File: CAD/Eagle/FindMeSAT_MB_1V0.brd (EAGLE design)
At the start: 99 x 49.2 mm, 128 parts, among them J291 MCX-J-P-X-RA-SM1, J685 SMA_CON, J701 MOLEX_105017-0001, J801 MICROSIM-8P_SDCARD-8P_MOLEX-1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, J901 JST_S3B-XH-A, Q101 ABS07-32.768KHZ, Q651 ABM3B-16MHZ-10-R50-1-U, U1001 CFPT-141-20MHZ, U101 ATXMEGA256A3BU-AU, U1011 OPA354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

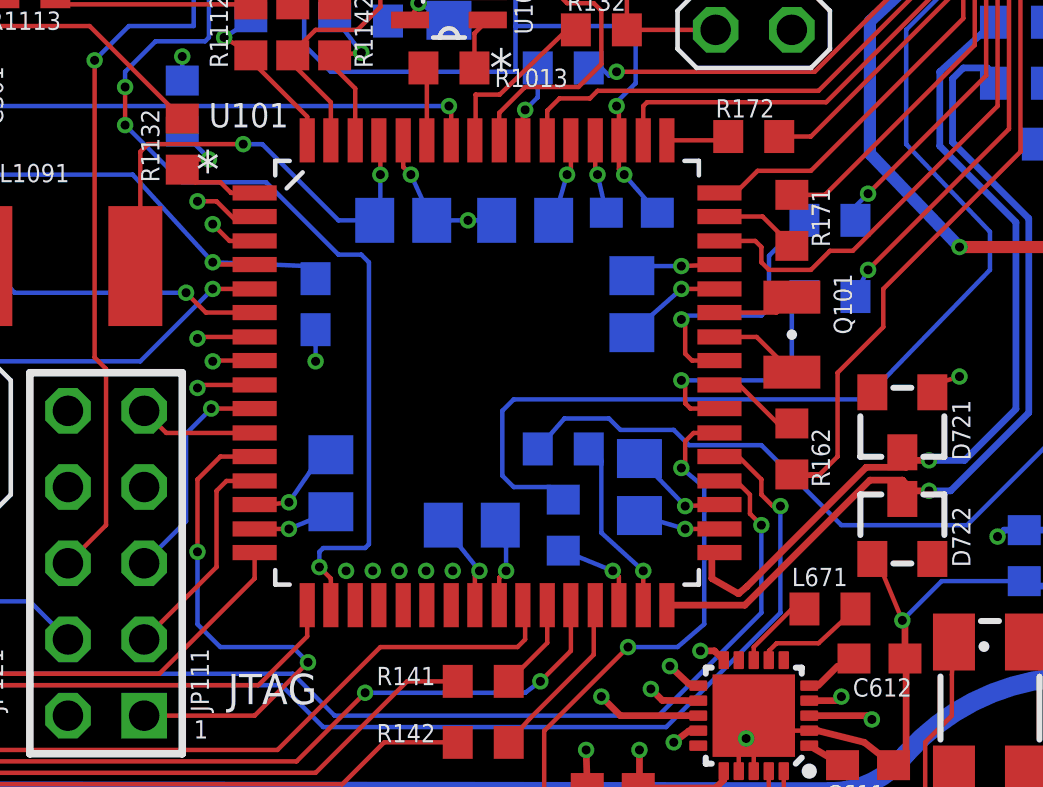
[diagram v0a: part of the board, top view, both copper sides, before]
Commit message: Eagle - I/O header needs OC1A for digital clock output, USB_ID gives way and goes to ADC1/ADC9/AC1 port
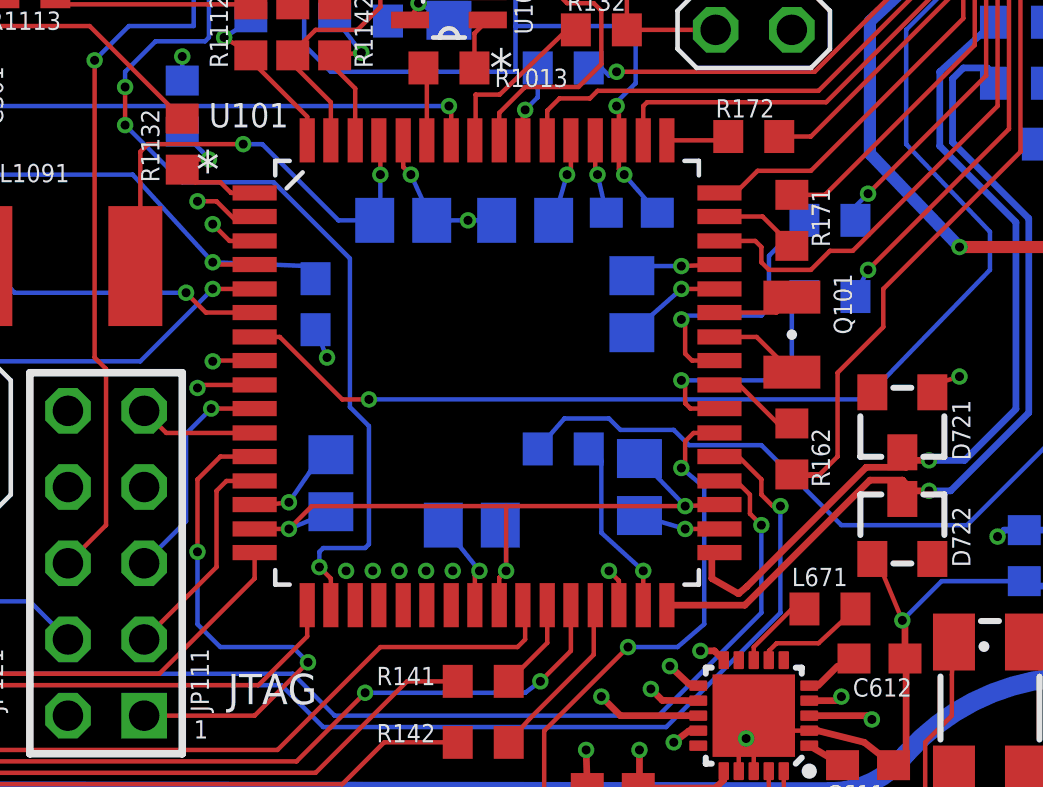
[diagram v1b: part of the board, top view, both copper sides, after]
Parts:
- removed R151: 27R, rcl:R0603
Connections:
- net IO_AD1 renamed IO_ADC4
- net IO_AD2 renamed IO_ADC5
- net IO_D2 renamed IO_DAC0
- net IO_D3 renamed IO_DAC1
- removed net IO_D1: JP181.2, U101.7
- removed net USB_ID_DRV: R151.1, U101.30
- new net IO_OC1A: JP181.2, U101.30
- net USB_ID: now also U101.7; no longer R151.2
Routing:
- net IO_OC1A: track 0.00 -> 29.0 mm, vias 0 -> 1
- net +3V3: track 69.9 -> 85.5 mm
- net IO_D1: track 12.8 -> 0.00 mm, vias 1 -> 0
- net USB_ID: track 38.0 -> 42.5 mm, vias 0 -> 1
- net USB_ID_DRV: track 3.01 -> 0.00 mm, vias 1 -> 0

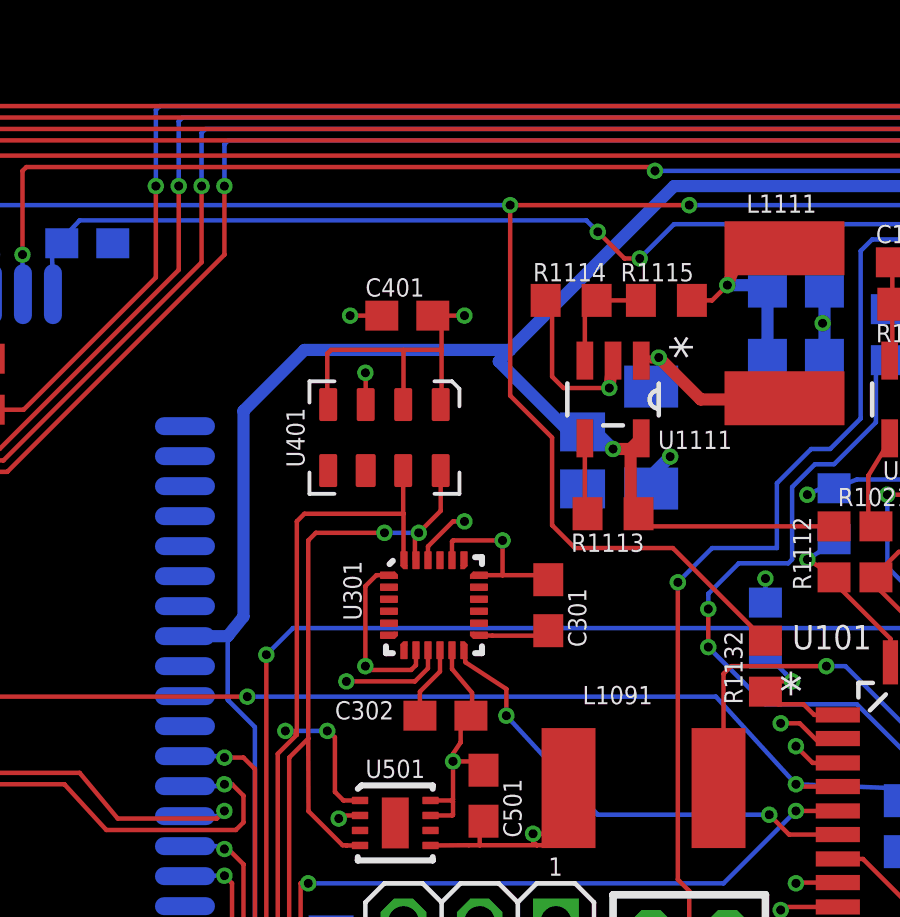
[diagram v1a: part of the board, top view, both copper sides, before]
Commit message: Eagle - I2C bus terminated
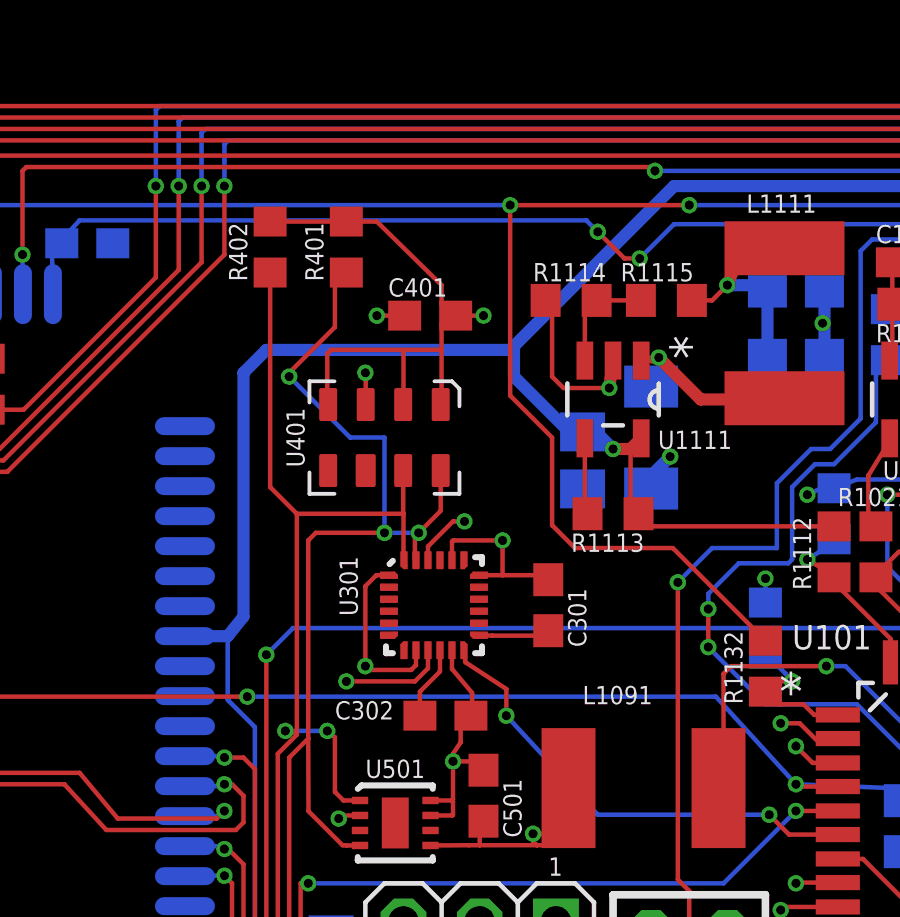
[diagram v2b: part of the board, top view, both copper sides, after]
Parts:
- added R401, R402: 10kR, rcl:R0603
- R211, R212: value 3.3kR -> 10kR
- moved C401 0.76 mm to (49.8, 34.5)
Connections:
- net +3V3: now also R401.2, R402.2
- net SCL1: now also R401.1
- net SDA1: now also R402.1
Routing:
- net SCL1: track 98.9 -> 110.3 mm, vias 7 -> 8
- net SDA1: track 96.1 -> 104.6 mm
- net +3V3: track 85.5 -> 93.5 mm
- net +5V: track 129.1 -> 129.6 mm

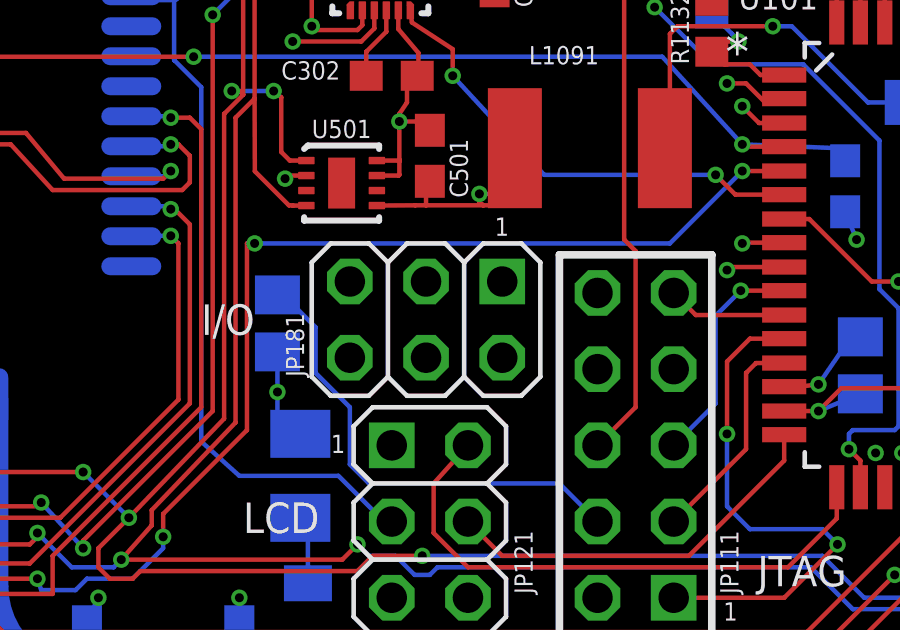
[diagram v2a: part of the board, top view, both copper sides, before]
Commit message: Eagle - dis-parted +3V3 layer by signal lines bridged, Beta-LAYOUT previews updated
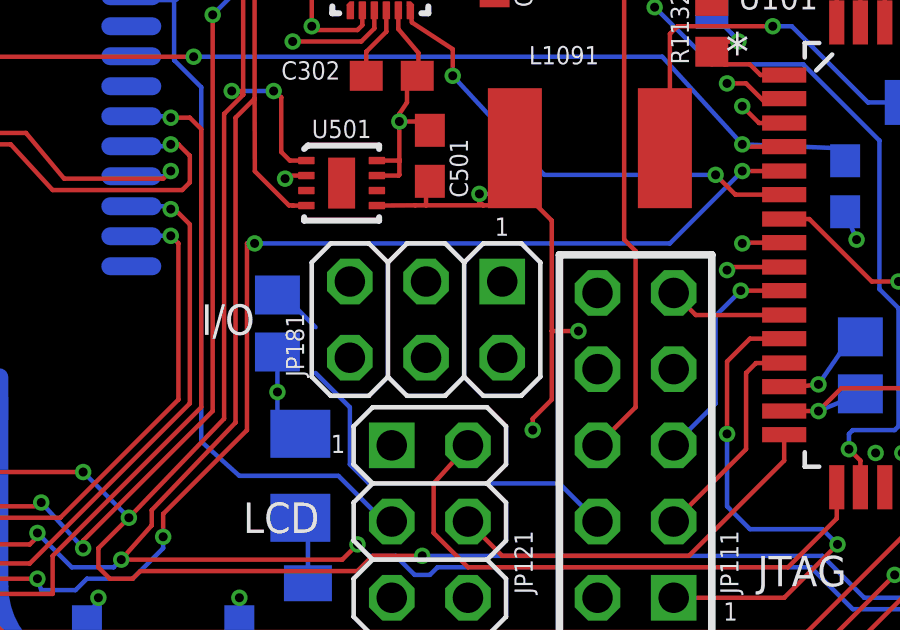
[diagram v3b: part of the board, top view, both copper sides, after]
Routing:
- net +3V3: track 93.5 -> 103.4 mm, vias 16 -> 18
- net VREF: track 15.8 -> 14.3 mm
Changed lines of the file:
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@@
 <layer number="19" name="Unrouted" color="6" fill="1" visible="yes" active="yes"/>
 <layer number="20" name="Dimension" color="15" fill="1" visible="yes" active="yes"/>
-<layer number="21" name="tPlace" color="7" fill="1" visible="yes" active="yes"/>
-<layer number="22" name="bPlace" color="7" fill="1" visible="yes" active="yes"/>
-<layer number="23" name="tOrigins" color="15" fill="1" visible="yes" active="yes"/>
-<layer number="24" name="bOrigins" color="15" fill="1" visible="yes" active="yes"/>
-<layer number="25" name="tNames" color="7" fill="1" visible="yes" active="yes"/>
-<layer number="26" name="bNames" color="7" fill="1" visible="yes" active="yes"/>
+<layer number="21" name="tPlace" color="7" fill="1" visible="no" active="yes"/>
+<layer number="22" name="bPlace" color="7" fill="1" visible="no" active="yes"/>
+<layer number="23" name="tOrigins" color="15" fill="1" visible="no" active="yes"/>
+<layer number="24" name="bOrigins" color="15" fill="1" visible="no" active="yes"/>
+<layer number="25" name="tNames" color="7" fill="1" visible="no" active="yes"/>
+<layer number="26" name="bNames" color="7" fill="1" visible="no" active="yes"/>
 <layer number="27" name="tValues" color="5" fill="1" visible="no" active="yes"/>
 <layer number="28" name="bValues" color="5" fill="1" visible="no" active="yes"/>
@@
 <wire x1="50.165" y1="34.925" x2="50.292" y2="34.925" width="0.15" layer="1"/>
 <wire x1="50.292" y1="34.925" x2="50.673" y2="34.544" width="0.15" layer="1"/>
+<wire x1="44.45" y1="37.68" x2="46.99" y2="37.68" width="0.15" layer="1"/>
+<wire x1="55.118" y1="16.891" x2="55.626" y2="16.383" width="0.15" layer="1"/>
+<wire x1="55.626" y1="16.383" x2="55.626" y2="12.7" width="0.15" layer="1"/>
+<wire x1="55.626" y1="12.7" x2="55.626" y2="10.414" width="0.15" layer="1"/>
+<wire x1="55.626" y1="10.414" x2="54.991" y2="9.779" width="0.15" layer="1"/>
+<wire x1="54.991" y1="9.779" x2="54.991" y2="9.398" width="0.15" layer="1"/>
+<wire x1="55.118" y1="16.891" x2="54.396" y2="16.891" width="0.15" layer="1"/>
+<wire x1="54.396" y1="16.891" x2="54.396" y2="17.272" width="0.15" layer="1"/>
+<via x="54.991" y="9.398" extent="1-16" drill="0.3" shape="octagon"/>
+<via x="56.515" y="12.7" extent="1-16" drill="0.3" shape="octagon"/>
+<wire x1="56.515" y1="12.7" x2="55.626" y2="12.7" width="0.15" layer="1"/>
 <wire x1="74.422" y1="28.868" x2="81.28" y2="31.75" width="0" layer="19" extent="1-1"/>
 <wire x1="69.85" y1="26.99" x2="74.08" y2="29.21" width="0" layer="19" extent="1-16"/>
@@
 <wire x1="76.2" y1="12.38" x2="75.946" y2="18.476" width="0" layer="19" extent="16-16"/>
 <wire x1="59.69" y1="11.43" x2="63.373" y2="10.033" width="0" layer="19" extent="1-1"/>
-<wire x1="76.2" y1="2.667" x2="71.5264" y2="7.493" width="0" layer="19" extent="1-1"/>
-<wire x1="51.562" y1="34.544" x2="58.508" y2="35.052" width="0" layer="19" extent="1-1"/>
+<wire x1="56.515" y1="12.7" x2="59.69" y2="11.43" width="0" layer="19" extent="1-1"/>
+<wire x1="53.721" y1="23.876" x2="53.721" y2="19.725" width="0" layer="19" extent="1-1"/>
+<wire x1="49.311" y1="23.392" x2="51.4635" y2="23.892" width="0" layer="19" extent="1-1"/>
+<wire x1="49.711" y1="26.392" x2="48.3585" y2="25.892" width="0" layer="19" extent="1-1"/>
+<wire x1="50.135" y1="31.58" x2="50.546" y2="27.686" width="0" layer="19" extent="1-1"/>
 <wire x1="46.99" y1="37.68" x2="46.99" y2="37.719" width="0" layer="19" extent="1-1"/>
-<wire x1="50.546" y1="27.686" x2="50.135" y2="31.58" width="0" layer="19" extent="1-1"/>
-<wire x1="48.3585" y1="25.892" x2="49.711" y2="26.392" width="0" layer="19" extent="1-1"/>
-<wire x1="51.4635" y1="23.892" x2="49.311" y2="23.392" width="0" layer="19" extent="1-1"/>
-<wire x1="53.721" y1="19.725" x2="53.721" y2="23.876" width="0" layer="19" extent="1-1"/>
 <wire x1="46.482" y1="12.004" x2="49.796" y2="16.883" width="0" layer="19" extent="1-16"/>
 <wire x1="50.292" y1="3.81" x2="46.99" y2="9.02" width="0" layer="19" extent="16-16"/>
+<wire x1="76.2" y1="2.667" x2="71.5264" y2="7.493" width="0" layer="19" extent="1-1"/>
 <wire x1="32.17" y1="7.835" x2="46.482" y2="9.528" width="0" layer="19" extent="16-16"/>
-<wire x1="44.45" y1="37.68" x2="46.99" y2="37.68" width="0.15" layer="1"/>
 </signal>
 <signal name="FB">
@@
 <wire x1="46.482" y1="13.904" x2="46.736" y2="13.843" width="0.15" layer="16"/>
 <wire x1="46.736" y1="13.843" x2="47.752" y2="12.827" width="0.15" layer="16"/>
-<wire x1="47.752" y1="12.827" x2="47.752" y2="11.303" width="0.15" layer="16"/>
 <wire x1="47.752" y1="11.303" x2="48.895" y2="10.16" width="0.15" layer="16"/>
 <wire x1="48.895" y1="10.16" x2="48.895" y2="8.255" width="0.15" layer="16"/>
@@
 <wire x1="49.53" y1="7.62" x2="55.88" y2="7.62" width="0.15" layer="16"/>
 <wire x1="55.88" y1="7.62" x2="57.15" y2="6.35" width="0.15" layer="16"/>
+<wire x1="47.752" y1="11.303" x2="47.752" y2="12.827" width="0" layer="19" extent="16-16"/>
 </signal>
 <signal name="GPS_RF_IN" class="2">

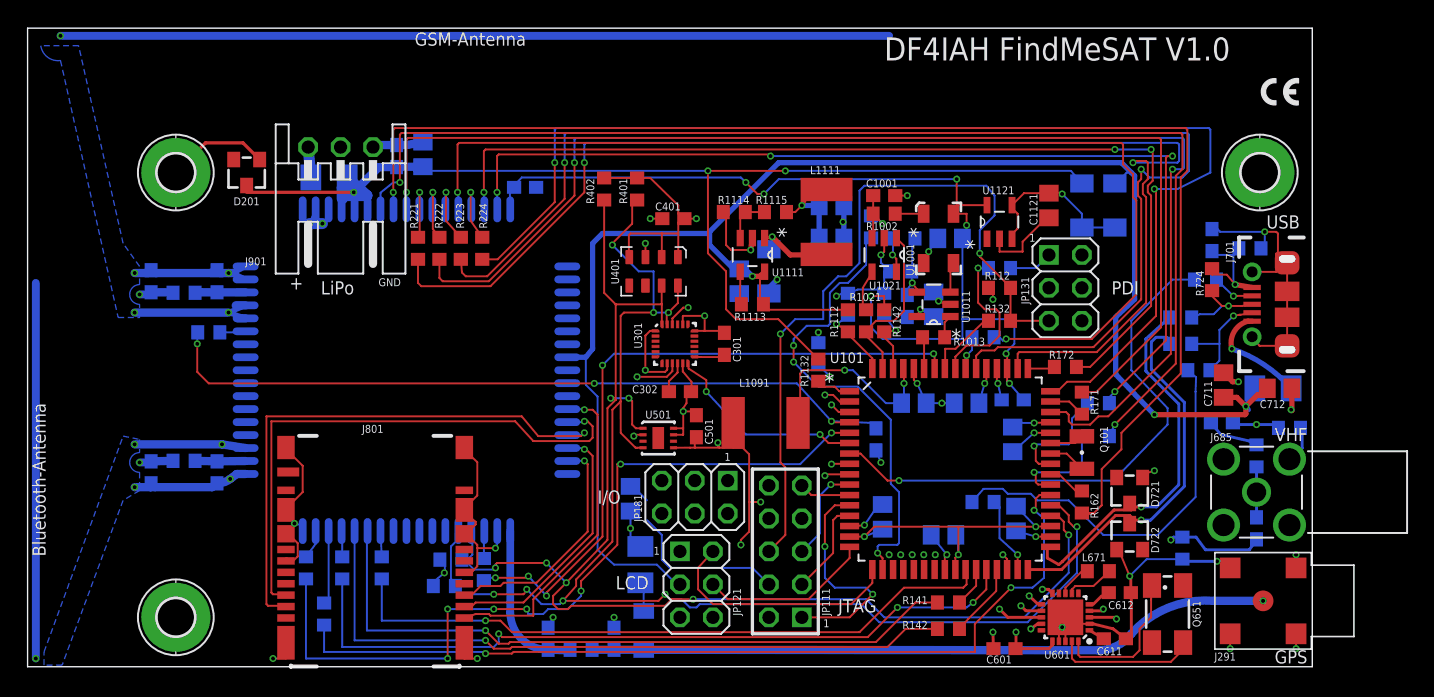
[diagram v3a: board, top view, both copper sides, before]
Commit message: Eagle - USB bus lines corrected, some airwires fixed
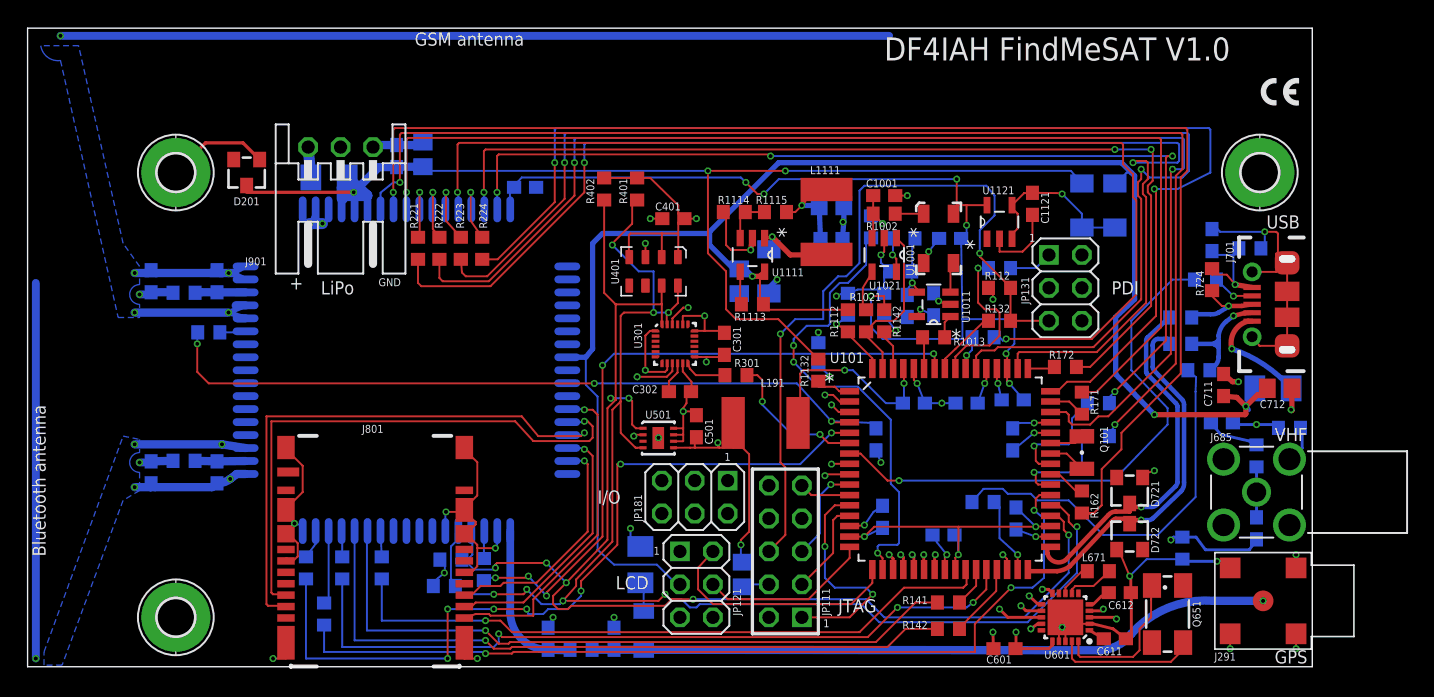
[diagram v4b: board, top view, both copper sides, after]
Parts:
- removed C1091, C1092, C1093, C1094, C1095, C1096: 100nF, rcl:C0805
- added C191, C192, C193, C194, C195, C196: 100nF, rcl:C0603
- added R301: 68R, rcl:R0603
- C1002, C1012, C1112, C1121, C711: device rcl:C0805 -> rcl:C0603
- R1013: value 10R -> 47R
- R131, R132, R141, R142, R151, R162, R163, R171, R172, R173, R221, R222, R223, R224, R231, R232, R233, R234, R241, R251: value 27R -> 68R
- RPOLY291: value 0A150 -> 50mA/150mA
- RPOLY711: value 1A0 -> 0.5A/1.0A
- RPOLY901: value 2.2A -> 1.1A/2.2A
- moved R111 10.4 mm to (55.1, 7.11), turned to 90 degrees
- moved C1121 1.28 mm to (77.5, 35.7)
- renumbered L1091 to L191, R152 to R151
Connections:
- new net MPU_INT: R301.1, U301.12
- net +3V3: now also C191.1, C192.1, C193.1, C194.1, C195.1; no longer C1091.1, C1092.1, C1093.1, C1094.1, C1095.1
- net AVCC: now also C196.1; no longer C1096.1
- net GND: now also C191.2, C192.2, C193.2, C194.2, C195.2, C196.2, U501.6; no longer C1091.2, C1092.2, C1093.2, C1094.2, C1095.2, C1096.2
- net I2C2_INT: now also R301.2; no longer U301.12
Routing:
- net VREF: track 14.3 -> 2.08 mm
- net GND: track 209.0 -> 213.9 mm, vias 50 -> 52
- net I2C2_INT: track 15.6 -> 11.2 mm
- net MPU_INT: track 0.00 -> 3.31 mm
- net AX_IRQ: track 14.3 -> 15.6 mm
- net AX_SEL: track 13.3 -> 14.5 mm
- net AX_MOSI: track 13.3 -> 14.5 mm
- net AX_CLK: track 13.3 -> 14.4 mm
- net AX_MISO: track 13.3 -> 14.4 mm
- net USB_D_P: track 29.3 -> 28.3 mm
- net USB_D_N: track 29.7 -> 28.8 mm
- net J_D-: track 8.53 -> 9.29 mm
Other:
- board text added: "Bluetooth antenna"
- board text added: "GSM antenna"
- board text removed: "Bluetooth-Antenna"
- board text removed: "GSM-Antenna"

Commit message: Eagle - Power connector mirrored, design *.dru file added
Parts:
- RPOLY291: device rcl:M1206 -> rcl:R1210
- moved C201 12.4 mm to (16.5, 36.1), flipped to the top, turned to 180 degrees
- moved C901 10.1 mm to (20.6, 37.7), turned to 0 degrees
- moved RPOLY901 1.40 mm to (24.6, 37.8), turned to 0 degrees
- moved D201 1.27 mm to (16.9, 39.4)
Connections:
- net BATTERY: now also J901.1; no longer J901.3
- net GND: now also J901.3; no longer J901.1
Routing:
- net GND: track 213.9 -> 223.1 mm, vias 52 -> 51
- net VBAT: track 100.1 -> 93.5 mm
- net GSM_VDD_EXT: track 92.7 -> 96.5 mm
